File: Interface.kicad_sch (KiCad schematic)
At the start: 19 parts, among them J1 Debugger, J2 USART, J3 SPI, J4 USB_C_Receptacle_USB2.0, Q1 Q_NMOS_GSD, U3 USBLC6-2SC6

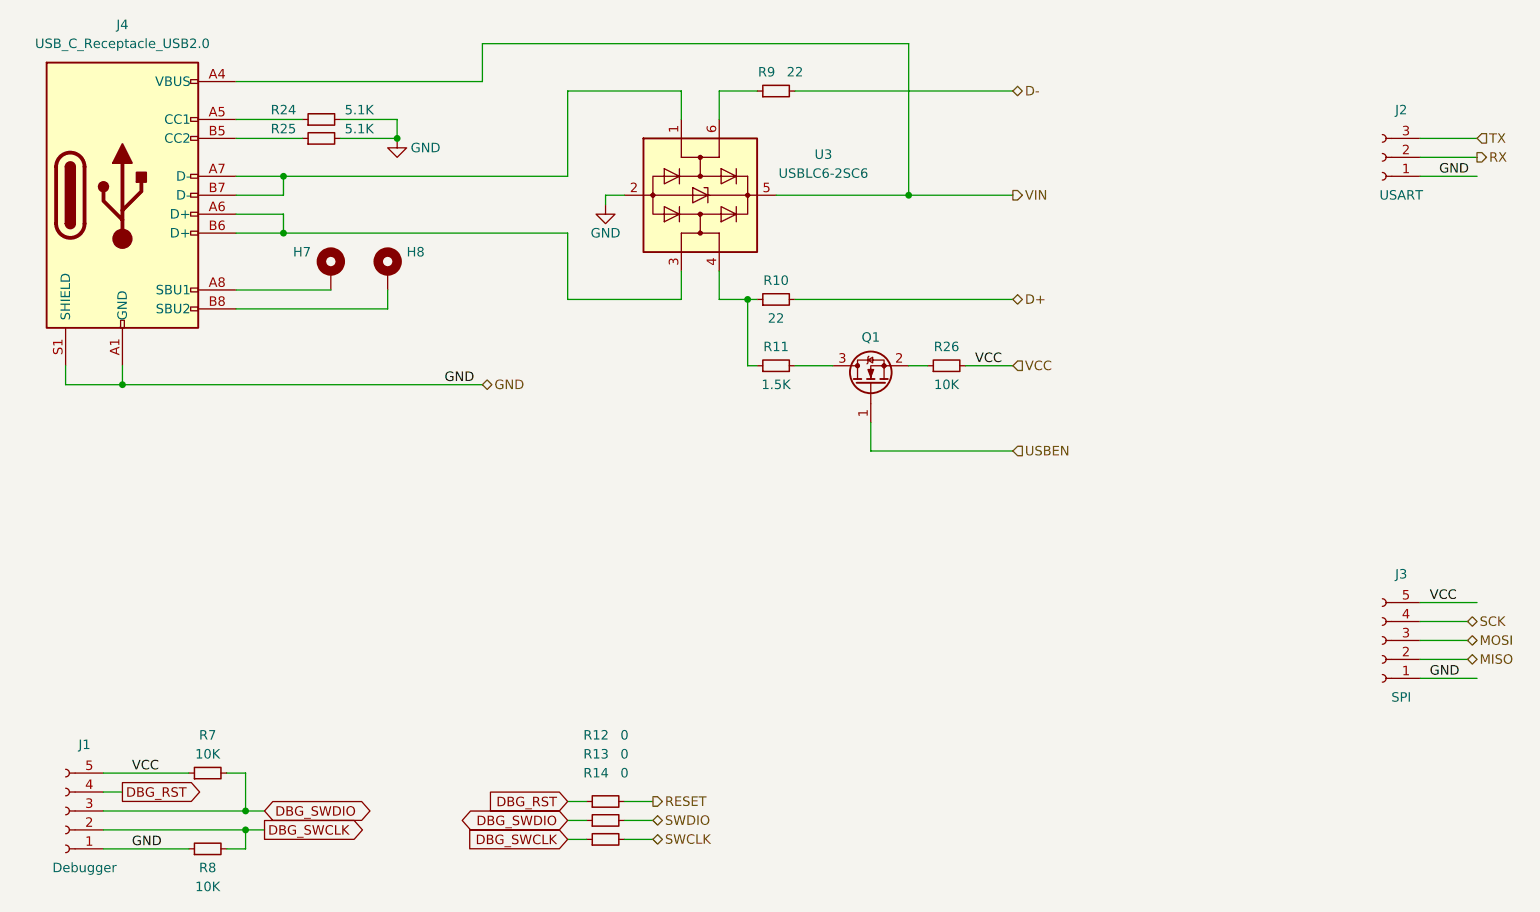
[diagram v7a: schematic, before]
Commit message: modify power/bootload circuit
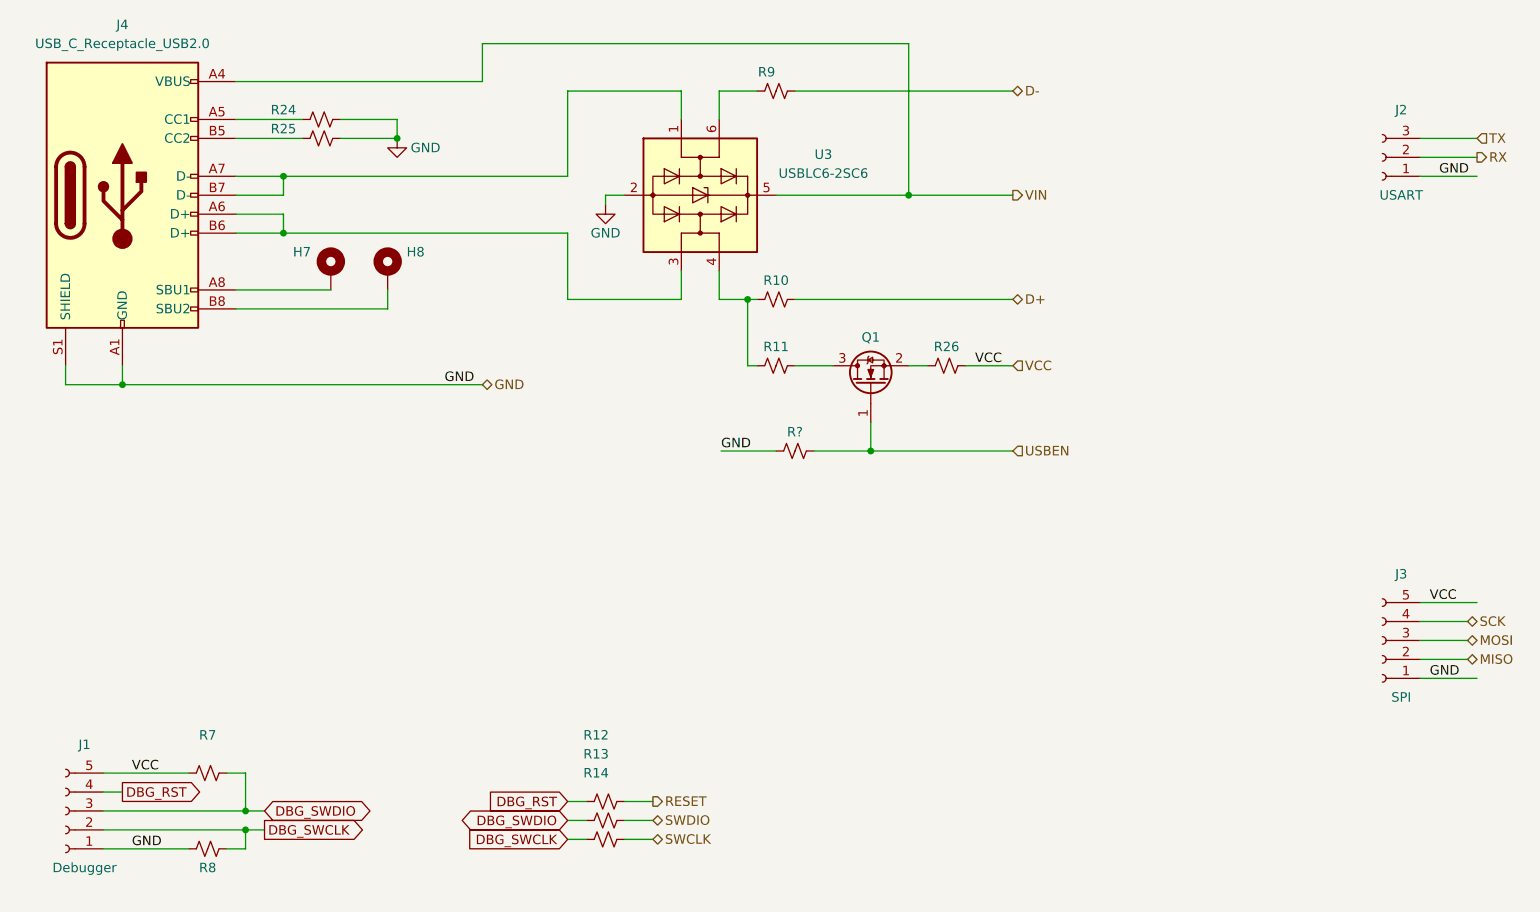
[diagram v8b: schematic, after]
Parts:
- added R?: (no value), symbol Device:R_Small_US
- R10, R9: value 22 -> (none); footprint Resistor_SMD:R_0603_1608Metric -> (none); symbol Device:R_Small -> Device:R_Small_US
- R11: value 1.5K -> (none); footprint Resistor_SMD:R_0603_1608Metric -> (none); symbol Device:R_Small -> Device:R_Small_US
- R12, R13, R14: value 0 -> (none); footprint Resistor_SMD:R_0603_1608Metric -> (none); symbol Device:R_Small -> Device:R_Small_US
- R24, R25: value 5.1K -> (none); footprint Resistor_SMD:R_0603_1608Metric -> (none); symbol Device:R_Small -> Device:R_Small_US
- R26, R7, R8: value 10K -> (none); footprint Resistor_SMD:R_0603_1608Metric -> (none); symbol Device:R_Small -> Device:R_Small_US
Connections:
- net GND: now also R?.1
- net USBEN: now also R?.2
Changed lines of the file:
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@@
   (junction (at 77.47 58.42) (diameter 0) (color 0 0 0 0)
   )
+  (junction (at 156.21 87.63) (diameter 0) (color 0 0 0 0)
+  )
   (junction (at 72.39 135.89) (diameter 0) (color 0 0 0 0)
   )
@@
     (stroke (width 0) (type default) (color 0 0 0 0))
   )
+  (wire (pts (xy 148.59 87.63) (xy 156.21 87.63))
+    (stroke (width 0) (type default) (color 0 0 0 0))
+  )
   (wire (pts (xy 229.87 107.95) (xy 237.49 107.95))
     (stroke (width 0) (type default) (color 0 0 0 0))
@@
     (stroke (width 0) (type default) (color 0 0 0 0))
   )
+  (wire (pts (xy 136.144 87.63) (xy 143.51 87.63))
+    (stroke (width 0) (type default) (color 0 0 0 0))
+  )
   (wire (pts (xy 72.39 140.97) (xy 72.39 138.43))
     (stroke (width 0) (type default) (color 0 0 0 0))
@@
   )
   (label "GND" (at 99.06 78.74 0)
+    (effects (font (size 1.27 1.27)) (justify left bottom))
+  )
+  (label "GND" (at 136.144 87.63 0)
     (effects (font (size 1.27 1.27)) (justify left bottom))
   )
@@
     (effects (font (size 1.27 1.27)) (justify left))
   )
-  (symbol (lib_id "Device:R_Small") (at 82.55 45.72 90) (unit 1)
+  (symbol (lib_id "Device:R_Small_US") (at 82.55 45.72 90) (unit 1)
     (in_bom yes) (on_board yes)
     (property "Reference" "R25" (id 0) (at 77.47 44.45 90))
-    (property "Value" "5.1K" (id 1) (at 87.63 44.45 90))
-    (property "Footprint" "Resistor_SMD:R_0603_1608Metric" (id 2) (at 82.55 45.72 0)
+    (property "Value" "" (id 1) (at 87.63 44.45 90))
+    (property "Footprint" "" (id 2) (at 82.55 45.72 0)
       (effects (font (size 1.27 1.27)) hide)
     )
@@
     (pin "6")
   )
-  (symbol (lib_id "Device:R_Small") (at 67.31 140.97 90) (unit 1)
+  (symbol (lib_id "Device:R_Small_US") (at 67.31 140.97 90) (unit 1)
     (in_bom yes) (on_board yes)
     (property "Reference" "R8" (id 0) (at 67.31 143.51 90))
-    (property "Value" "10K" (id 1) (at 67.31 146.05 90))
-    (property "Footprint" "Resistor_SMD:R_0603_1608Metric" (id 2) (at 67.31 140.97 0)
+    (property "Value" "" (id 1) (at 67.31 146.05 90))
+    (property "Footprint" "" (id 2) (at 67.31 140.97 0)
       (effects (font (size 1.27 1.27)) hide)
     )
@@
     (pin "1")
   )
-  (symbol (lib_id "Device:R_Small") (at 143.51 76.2 90) (unit 1)
+  (symbol (lib_id "Device:R_Small_US") (at 143.51 76.2 90) (unit 1)
     (in_bom yes) (on_board yes)
     (property "Reference" "R11" (id 0) (at 143.51 73.66 90))
-    (property "Value" "1.5K" (id 1) (at 143.51 78.74 90))
-    (property "Footprint" "Resistor_SMD:R_0603_1608Metric" (id 2) (at 143.51 76.2 0)
+    (property "Value" "" (id 1) (at 143.51 78.74 90))
+    (property "Footprint" "" (id 2) (at 143.51 76.2 0)
       (effects (font (size 1.27 1.27)) hide)
     )
@@
     (pin "2")
   )
-  (symbol (lib_id "Device:R_Small") (at 120.65 139.7 90) (unit 1)
+  (symbol (lib_id "Device:R_Small_US") (at 120.65 139.7 90) (unit 1)
     (in_bom yes) (on_board yes)
     (property "Reference" "R14" (id 0) (at 119.38 130.81 90))
-    (property "Value" "0" (id 1) (at 123.19 130.81 90))
-    (property "Footprint" "Resistor_SMD:R_0603_1608Metric" (id 2) (at 120.65 139.7 0)
+    (property "Value" "" (id 1) (at 123.19 130.81 90))
+    (property "Footprint" "" (id 2) (at 120.65 139.7 0)
       (effects (font (size 1.27 1.27)) hide)
     )
@@
     (pin "5")
   )
-  (symbol (lib_id "Device:R_Small") (at 82.55 43.18 90) (unit 1)
+  (symbol (lib_id "Device:R_Small_US") (at 82.55 43.18 90) (unit 1)
     (in_bom yes) (on_board yes)
     (property "Reference" "R24" (id 0) (at 77.47 41.91 90))
-    (property "Value" "5.1K" (id 1) (at 87.63 41.91 90))
-    (property "Footprint" "Resistor_SMD:R_0603_1608Metric" (id 2) (at 82.55 43.18 0)
+    (property "Value" "" (id 1) (at 87.63 41.91 90))
+    (property "Footprint" "" (id 2) (at 82.55 43.18 0)
       (effects (font (size 1.27 1.27)) hide)
     )
@@
     (pin "2")
   )
-  (symbol (lib_id "Device:R_Small") (at 166.37 76.2 90) (unit 1)
+  (symbol (lib_id "Device:R_Small_US") (at 166.37 76.2 90) (unit 1)
     (in_bom yes) (on_board yes)
     (property "Reference" "R26" (id 0) (at 166.37 73.66 90))
-    (property "Value" "10K" (id 1) (at 166.37 78.74 90))
-    (property "Footprint" "Resistor_SMD:R_0603_1608Metric" (id 2) (at 166.37 76.2 0)
+    (property "Value" "" (id 1) (at 166.37 78.74 90))
+    (property "Footprint" "" (id 2) (at 166.37 76.2 0)
       (effects (font (size 1.27 1.27)) hide)
     )
@@
     (pin "5")
   )
-  (symbol (lib_id "Device:R_Small") (at 120.65 134.62 90) (unit 1)
+  (symbol (lib_id "Device:R_Small_US") (at 120.65 134.62 90) (unit 1)
     (in_bom yes) (on_board yes)
     (property "Reference" "R12" (id 0) (at 119.38 125.73 90))
-    (property "Value" "0" (id 1) (at 123.19 125.73 90))
-    (property "Footprint" "Resistor_SMD:R_0603_1608Metric" (id 2) (at 120.65 134.62 0)
+    (property "Value" "" (id 1) (at 123.19 125.73 90))
+    (property "Footprint" "" (id 2) (at 120.65 134.62 0)
       (effects (font (size 1.27 1.27)) hide)
     )
@@
     (pin "2")
   )
-  (symbol (lib_id "Device:R_Small") (at 67.31 130.81 90) (unit 1)
+  (symbol (lib_id "Device:R_Small_US") (at 67.31 130.81 90) (unit 1)
     (in_bom yes) (on_board yes)
     (property "Reference" "R7" (id 0) (at 67.31 125.73 90))
-    (property "Value" "10K" (id 1) (at 67.31 128.27 90))
-    (property "Footprint" "Resistor_SMD:R_0603_1608Metric" (id 2) (at 67.31 130.81 0)
+    (property "Value" "" (id 1) (at 67.31 128.27 90))
+    (property "Footprint" "" (id 2) (at 67.31 130.81 0)
       (effects (font (size 1.27 1.27)) hide)
     )
     (property "Datasheet" "~" (id 3) (at 67.31 130.81 0)
+      (effects (font (size 1.27 1.27)) hide)
+    )
+    (pin "1")
+    (pin "2")
+  )
+  (symbol (lib_id "Device:R_Small_US") (at 146.05 87.63 90) (unit 1)
+    (in_bom yes) (on_board yes)
+    (property "Reference" "R?" (id 0) (at 146.05 85.09 90))
+    (property "Value" "" (id 1) (at 146.05 90.17 90))
+    (property "Footprint" "" (id 2) (at 146.05 87.63 0)
+      (effects (font (size 1.27 1.27)) hide)
+    )
+    (property "Datasheet" "~" (id 3) (at 146.05 87.63 0)
       (effects (font (size 1.27 1.27)) hide)
     )
@@
     (pin "1")
   )
-  (symbol (lib_id "Device:R_Small") (at 120.65 137.16 90) (unit 1)
+  (symbol (lib_id "Device:R_Small_US") (at 120.65 137.16 90) (unit 1)
     (in_bom yes) (on_board yes)
     (property "Reference" "R13" (id 0) (at 119.38 128.27 90))
-    (property "Value" "0" (id 1) (at 123.19 128.27 90))
-    (property "Footprint" "Resistor_SMD:R_0603_1608Metric" (id 2) (at 120.65 137.16 0)
+    (property "Value" "" (id 1) (at 123.19 128.27 90))
+    (property "Footprint" "" (id 2) (at 120.65 137.16 0)
       (effects (font (size 1.27 1.27)) hide)
     )
@@
     (pin "2")
   )
-  (symbol (lib_id "Device:R_Small") (at 143.51 39.37 90) (unit 1)
+  (symbol (lib_id "Device:R_Small_US") (at 143.51 39.37 90) (unit 1)
     (in_bom yes) (on_board yes)
     (property "Reference" "R9" (id 0) (at 142.24 36.83 90))
-    (property "Value" "22" (id 1) (at 146.05 36.83 90))
-    (property "Footprint" "Resistor_SMD:R_0603_1608Metric" (id 2) (at 143.51 39.37 0)
+    (property "Value" "" (id 1) (at 146.05 36.83 90))
+    (property "Footprint" "" (id 2) (at 143.51 39.37 0)
       (effects (font (size 1.27 1.27)) hide)
     )
@@
     (pin "2")
   )
-  (symbol (lib_id "Device:R_Small") (at 143.51 67.31 90) (unit 1)
+  (symbol (lib_id "Device:R_Small_US") (at 143.51 67.31 90) (unit 1)
     (in_bom yes) (on_board yes)
     (property "Reference" "R10" (id 0) (at 143.51 64.77 90))
-    (property "Value" "22" (id 1) (at 143.51 69.85 90))
-    (property "Footprint" "Resistor_SMD:R_0603_1608Metric" (id 2) (at 143.51 67.31 0)
-      (effects (font (size 1.27 1.27)) hide)
-    )
+    (property "Value" "" (id 1) (at 143.51 69.85 90))
+    (property "Footprint" "" (id 2) (at 143.51 67.31 0)
+      (effects (font (size 1.27 1.27)) hide)
+    )
